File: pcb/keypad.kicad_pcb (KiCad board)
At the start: 2 copper layers, 148 x 103 mm, 54 parts, among them J1 Conn_02x06_Odd_Even, SW1 SW_Push, SW10 SW_Push, SW11 SW_Push, SW12 SW_Push, SW13 SW_Push, SW14 SW_Push, SW15 SW_Push, SW16 SW_Push, SW17 SW_Push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

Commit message: - Added a reset button for the controller  - Moved the through-hole diodes to not interfere with the switches
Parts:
- added SW_RST1: SW_Push, Button_Switch_THT:SW_PUSH_6mm_H7.3mm, F.Cu at (74.8, 18.0)
- moved D15 14.6 mm to (59.0, 93.8), turned to 90 degrees
- moved D19 14.3 mm to (140.0, 93.8), turned to 90 degrees
- moved D16 13.0 mm to (79.0, 93.8), turned to 90 degrees
- moved D17 12.9 mm to (98.0, 93.8), turned to 90 degrees
- moved D18 12.9 mm to (117.0, 93.8), turned to 90 degrees
- moved D20 2.85 mm to (56.0, 114.0)
- moved D21 2.85 mm to (85.2, 114.0)
- moved D22 2.85 mm to (114.4, 114.0)
- moved D1 2.00 mm to (28.0, 56.0)
- moved D2 2.00 mm to (47.1, 56.0)
- moved D3 2.00 mm to (66.1, 56.0)
- moved D4 2.00 mm to (85.2, 56.0)
- moved D5 2.00 mm to (104.2, 56.0)
- moved D6 2.00 mm to (123.3, 56.0)
- moved D7 2.00 mm to (142.3, 56.0)
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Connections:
- net /3.3v renamed /5v
- U1 pad 22: unconnected-(U1-Pad22) -> Net-(U1-Pad22)
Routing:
- net Net-(U1-Pad22): track 0.00 -> 85.2 mm
- net /Col2: track 223.5 -> 211.7 mm
- net /Col3: track 214.9 -> 206.8 mm
- net /Col1: track 299.3 -> 305.4 mm
- net /Col0: track 239.4 -> 245.2 mm
- net Net-(D18-Pad2): track 12.3 -> 6.81 mm
- net Net-(D17-Pad2): track 12.3 -> 6.83 mm
- net Net-(D16-Pad2): track 12.3 -> 6.85 mm
- net Net-(D15-Pad2): track 12.4 -> 7.51 mm
- net Net-(D19-Pad2): track 12.3 -> 7.39 mm
- net Net-(D22-Pad2): track 12.3 -> 15.3 mm
- net Net-(D21-Pad2): track 12.3 -> 15.1 mm
- net Net-(D20-Pad2): track 12.3 -> 15.1 mm
- net /Col5: track 156.7 -> 154.7 mm
- net Net-(D7-Pad2): track 12.3 -> 14.3 mm
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
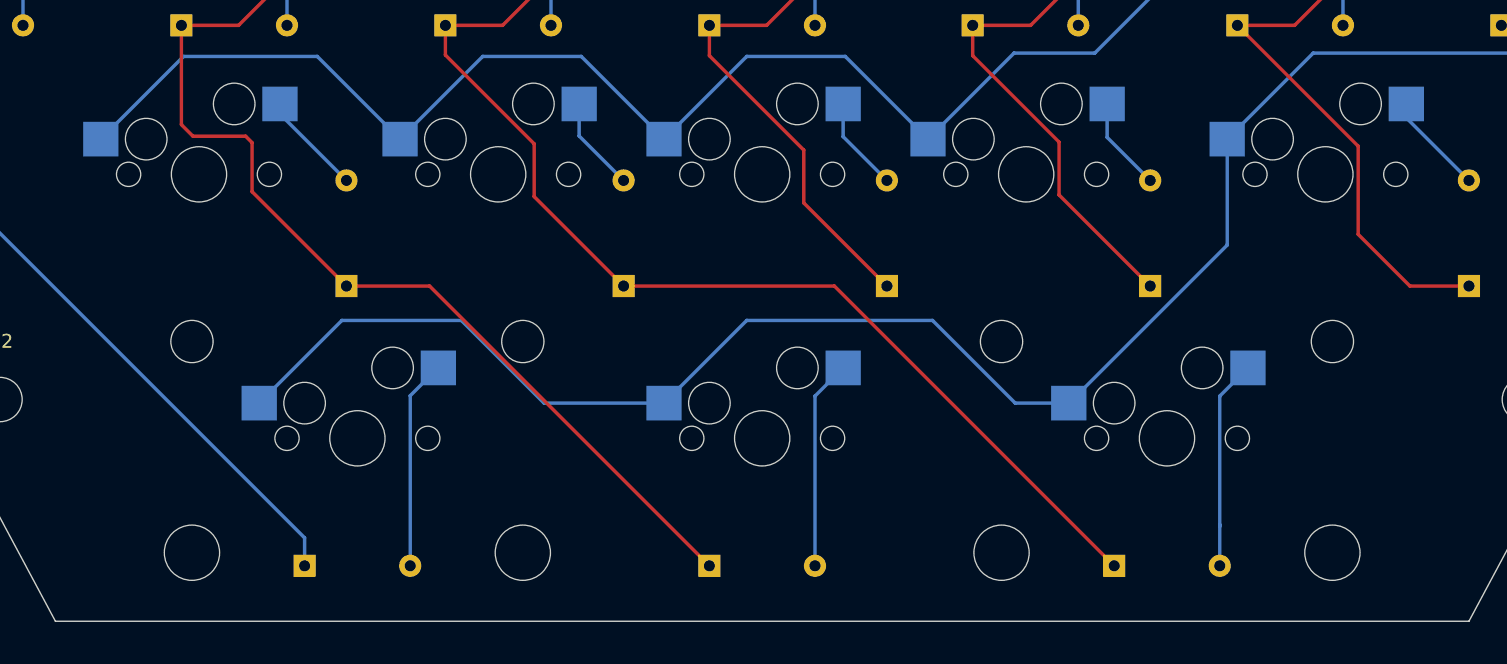
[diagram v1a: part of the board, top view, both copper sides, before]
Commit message: - Added plate details  - Fixed the spacing of non-1U keys on the PCB layout
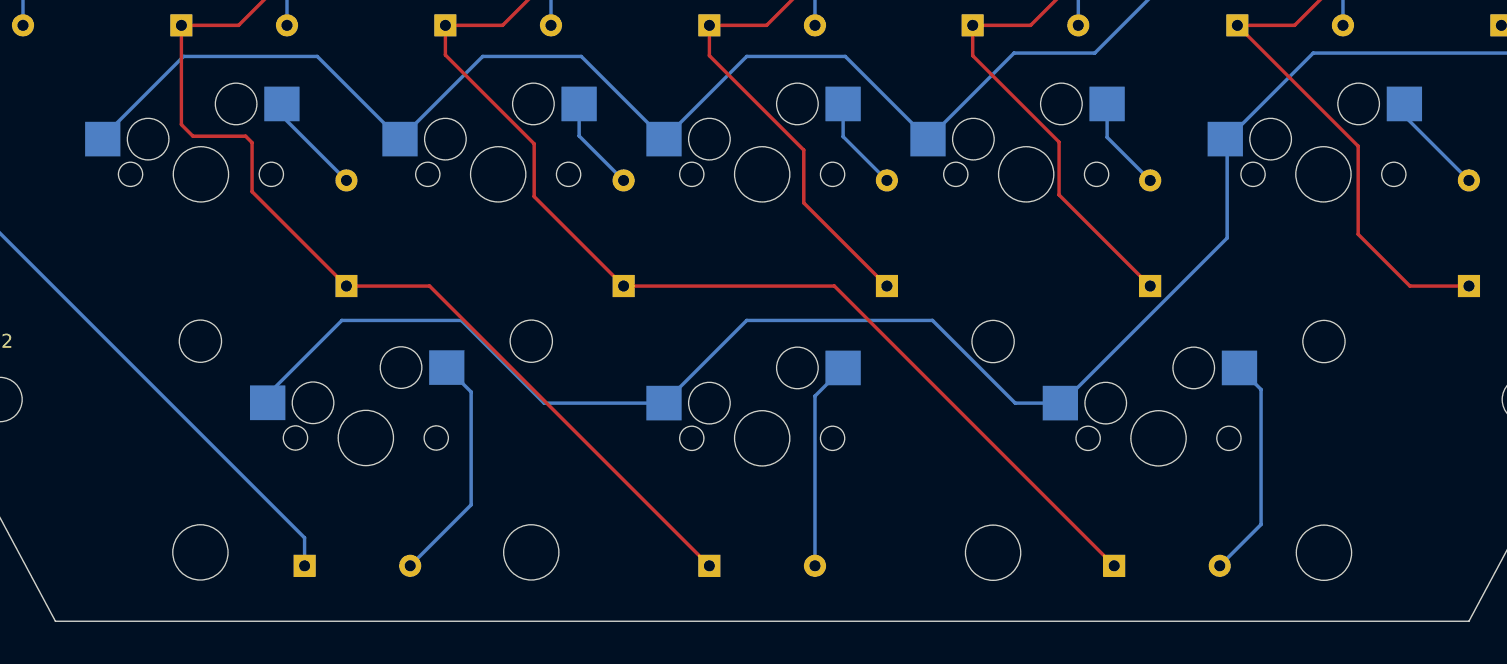
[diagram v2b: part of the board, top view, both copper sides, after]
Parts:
- moved SW20 0.61 mm to (60.4, 104.8)
- moved SW22 0.61 mm to (117.6, 104.8)
- moved SW15 0.14 mm to (48.5, 85.8)
- moved SW19 0.14 mm to (129.5, 85.8)
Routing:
- net Net-(D20-Pad2): track 15.1 -> 16.9 mm
- net Net-(D22-Pad2): track 15.3 -> 16.2 mm
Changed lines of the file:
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@@
   (net 22 "unconnected-(U1-Pad24)")
   (net 23 "/GND")
-  (net 24 "Net-(U1-Pad22)")
+  (net 24 "Net-(SW_RST1-Pad1)")
   (net 25 "unconnected-(U1-Pad1)")
   (net 26 "Net-(D10-Pad2)")
@@
   (net 48 "unconnected-(U1-Pad20)")
   (footprint "MX_Only:MXOnly-2U-Hotswap" (layer "F.Cu")
-    (at 59.79 104.8)
+    (at 60.4 104.77555)
     (property "Sheetfile" "keypad.kicad_sch")
     (property "Sheetname" "")
@@
   )
   (footprint "MX_Only:MXOnly-1.25U-Hotswap" (layer "F.Cu")
-    (at 48.36 85.75)
+    (at 48.5 85.75)
     (property "Sheetfile" "keypad.kicad_sch")
     (property "Sheetname" "")
@@
     (fp_circle (center 3.25 2.25) (end 1.25 2.5) (layer "F.Fab") (width 0.1) (fill none))
     (pad "1" thru_hole circle (at 6.5 0 90) (size 2 2) (drill 1.1) (layers *.Cu *.Mask)
-      (net 24 "Net-(U1-Pad22)") (pinfunction "1") (pintype "passive"))
+      (net 24 "Net-(SW_RST1-Pad1)") (pinfunction "1") (pintype "passive"))
     (pad "1" thru_hole circle (at 0 0 90) (size 2 2) (drill 1.1) (layers *.Cu *.Mask)
-      (net 24 "Net-(U1-Pad22)") (pinfunction "1") (pintype "passive"))
+      (net 24 "Net-(SW_RST1-Pad1)") (pinfunction "1") (pintype "passive"))
     (pad "2" thru_hole circle (at 0 4.5 90) (size 2 2) (drill 1.1) (layers *.Cu *.Mask)
       (net 23 "/GND") (pinfunction "2") (pintype "passive"))
@@
   )
   (footprint "MX_Only:MXOnly-2U-Hotswap" (layer "F.Cu")
-    (at 118.21 104.8)
+    (at 117.6 104.8)
     (property "Sheetfile" "keypad.kicad_sch")
     (property "Sheetname" "")
@@
   )
   (footprint "MX_Only:MXOnly-1.25U-Hotswap" (layer "F.Cu")
-    (at 129.64 85.75)
+    (at 129.5 85.75)
     (property "Sheetfile" "keypad.kicad_sch")
     (property "Sheetname" "")
@@
       (net 21 "/5v") (pinfunction "VCC") (pintype "power_in"))
     (pad "22" thru_hole oval locked (at 0 22.86 90) (size 1.6 1.6) (drill 0.8) (layers *.Cu *.Mask)
-      (net 24 "Net-(U1-Pad22)") (pinfunction "RST") (pintype "input"))
+      (net 24 "Net-(SW_RST1-Pad1)") (pinfunction "RST") (pintype "input"))
     (pad "23" thru_hole oval locked (at 0 25.4 90) (size 1.6 1.6) (drill 0.8) (layers *.Cu *.Mask)
       (net 23 "/GND") (pinfunction "GND") (pintype "power_in"))
@@
   (segment (start 90.5 18) (end 97 18) (width 0.25) (layer "B.Cu") (net 18))
   (segment (start 128.765 77) (end 122.555 83.21) (width 0.25) (layer "B.Cu") (net 18))
+  (segment (start 122.555 90.345) (end 122.555 83.21) (width 0.25) (layer "B.Cu") (net 18))
+  (segment (start 122.555 90.345) (end 110.64 102.26) (width 0.25) (layer "B.Cu") (net 18))
   (segment (start 135.45 20.45) (end 135.55 20.45) (width 0.25) (layer "B.Cu") (net 18))
   (segment (start 121.365 29) (end 121.365 37.728604) (width 0.25) (layer "B.Cu") (net 18))
@@
   (segment (start 135.45 20.45) (end 129.915 20.45) (width 0.25) (layer "B.Cu") (net 18))
   (segment (start 128 24) (end 131.55 20.45) (width 0.25) (layer "B.Cu") (net 18))
-  (segment (start 122.555 90.855) (end 122.555 83.21) (width 0.25) (layer "B.Cu") (net 18))
   (segment (start 152.109188 38.1) (end 154.042 40.032812) (width 0.25) (layer "B.Cu") (net 18))
-  (segment (start 111.15 102.26) (end 122.555 90.855) (width 0.25) (layer "B.Cu") (net 18))
   (segment (start 121.736396 38.1) (end 152.109188 38.1) (width 0.25) (layer "B.Cu") (net 18))
   (segment (start 58.673302 96.291698) (end 67.291698 96.291698) (width 0.25) (layer "B.Cu") (net 18))
@@
   (segment (start 67.291698 96.291698) (end 73.26 102.26) (width 0.25) (layer "B.Cu") (net 18))
   (segment (start 131.55 20.45) (end 135.45 20.45) (width 0.25) (layer "B.Cu") (net 18))
-  (segment (start 111.125 102.26) (end 111.15 102.26) (width 0.25) (layer "B.Cu") (net 18))
   (segment (start 101.291698 96.291698) (end 107.26 102.26) (width 0.25) (layer "B.Cu") (net 18))
   (segment (start 107.26 102.26) (end 111.125 102.26) (width 0.25) (layer "B.Cu") (net 18))
   (segment (start 87.883302 96.291698) (end 101.291698 96.291698) (width 0.25) (layer "B.Cu") (net 18))
+  (segment (start 110.64 102.26) (end 110.515 102.26) (width 0.25) (layer "B.Cu") (net 18))
   (segment (start 97 18) (end 101.5 18) (width 0.25) (layer "B.Cu") (net 18))
   (segment (start 149.550991 77) (end 128.765 77) (width 0.25) (layer "B.Cu") (net 18))
@@
   (segment (start 135.482 81.672) (end 135.482 80.67) (width 0.25) (layer "B.Cu") (net 35))
   (segment (start 140 86.19) (end 135.482 81.672) (width 0.25) (layer "B.Cu") (net 35))
-  (segment (start 65.632 99.72) (end 65.607 99.72) (width 0.25) (layer "B.Cu") (net 36))
-  (segment (start 65.607 99.72) (end 63.6 101.727) (width 0.25) (layer "B.Cu") (net 36))
-  (segment (start 63.6 101.727) (end 63.6 114) (width 0.25) (layer "B.Cu") (net 36))
+  (segment (start 68 101.45355) (end 68 109.6) (width 0.25) (layer "B.Cu") (net 36))
+  (segment (start 68 109.6) (end 63.6 114) (width 0.25) (layer "B.Cu") (net 36))
+  (segment (start 66.242 99.69555) (end 68 101.45355) (width 0.25) (layer "B.Cu") (net 36))
   (segment (start 108 25.69) (end 108.56 26.25) (width 0.25) (layer "B.Cu") (net 37))
   (segment (start 108 22.5) (end 108 25.69) (width 0.25) (layer "B.Cu") (net 37))
@@
   (segment (start 56.742 61.62) (end 54.71 63.652) (width 0.25) (layer "B.Cu") (net 39))
   (segment (start 54.71 63.652) (end 54.71 75) (width 0.25) (layer "B.Cu") (net 39))
-  (segment (start 122.02 101.752) (end 122.02 111.15) (width 0.25) (layer "B.Cu") (net 40))
-  (segment (start 122.02 114) (end 122.02 111.02) (width 0.25) (layer "B.Cu") (net 40))
-  (segment (start 124.052 99.72) (end 122.02 101.752) (width 0.25) (layer "B.Cu") (net 40))
+  (segment (start 125 111.02) (end 122.02 114) (width 0.25) (layer "B.Cu") (net 40))
+  (segment (start 123.442 99.72) (end 125 101.278) (width 0.25) (layer "B.Cu") (net 40))
+  (segment (start 125 101.278) (end 125 111.02) (width 0.25) (layer "B.Cu") (net 40))
   (segment (start 97 22.5) (end 97 25.69) (width 0.25) (layer "B.Cu") (net 43))
   (segment (start 97 25.69) (end 97.56 26.25) (width 0.25) (layer "B.Cu") (net 43))

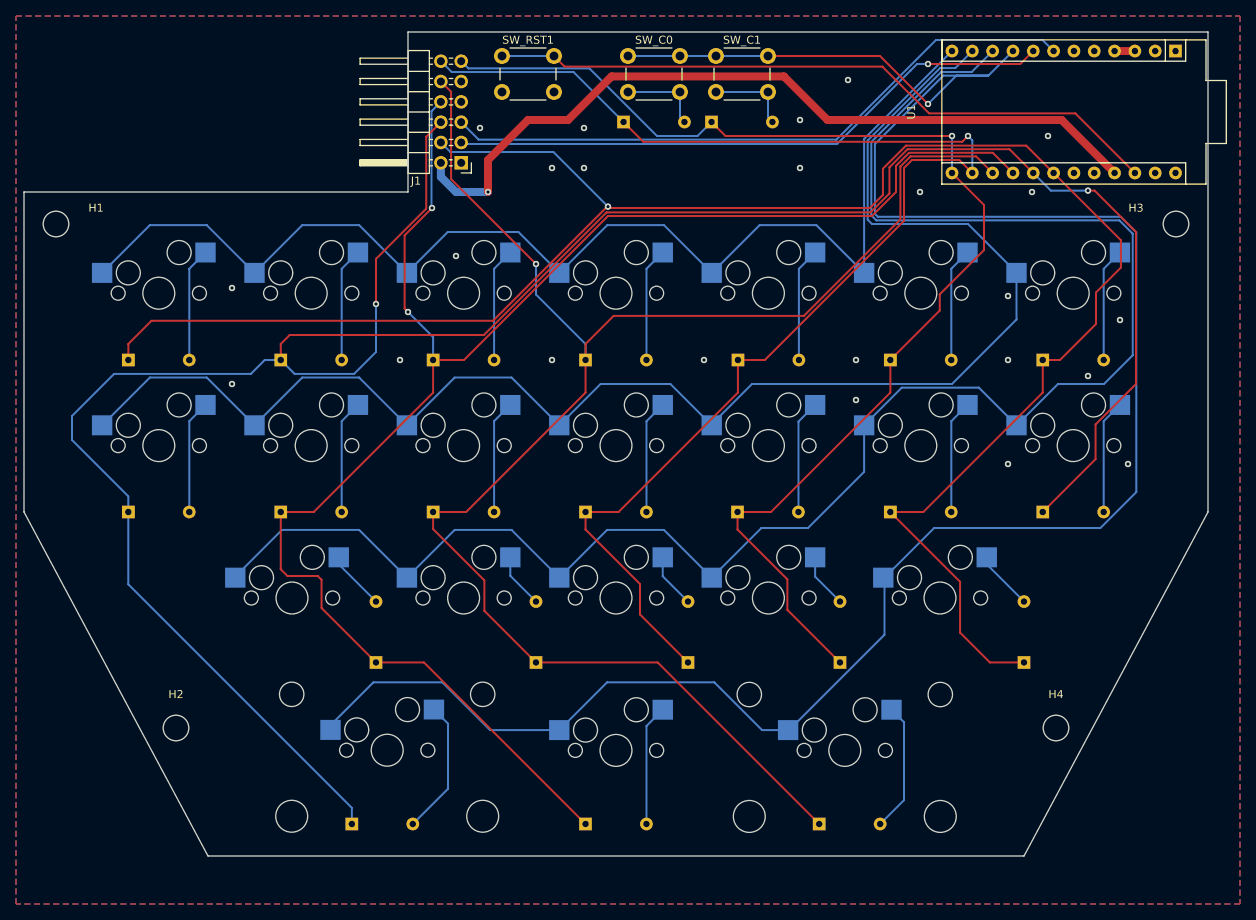
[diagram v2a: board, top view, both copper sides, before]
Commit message: - Switched to the KB2040  - Modified the pin header to remove some silk screen sections
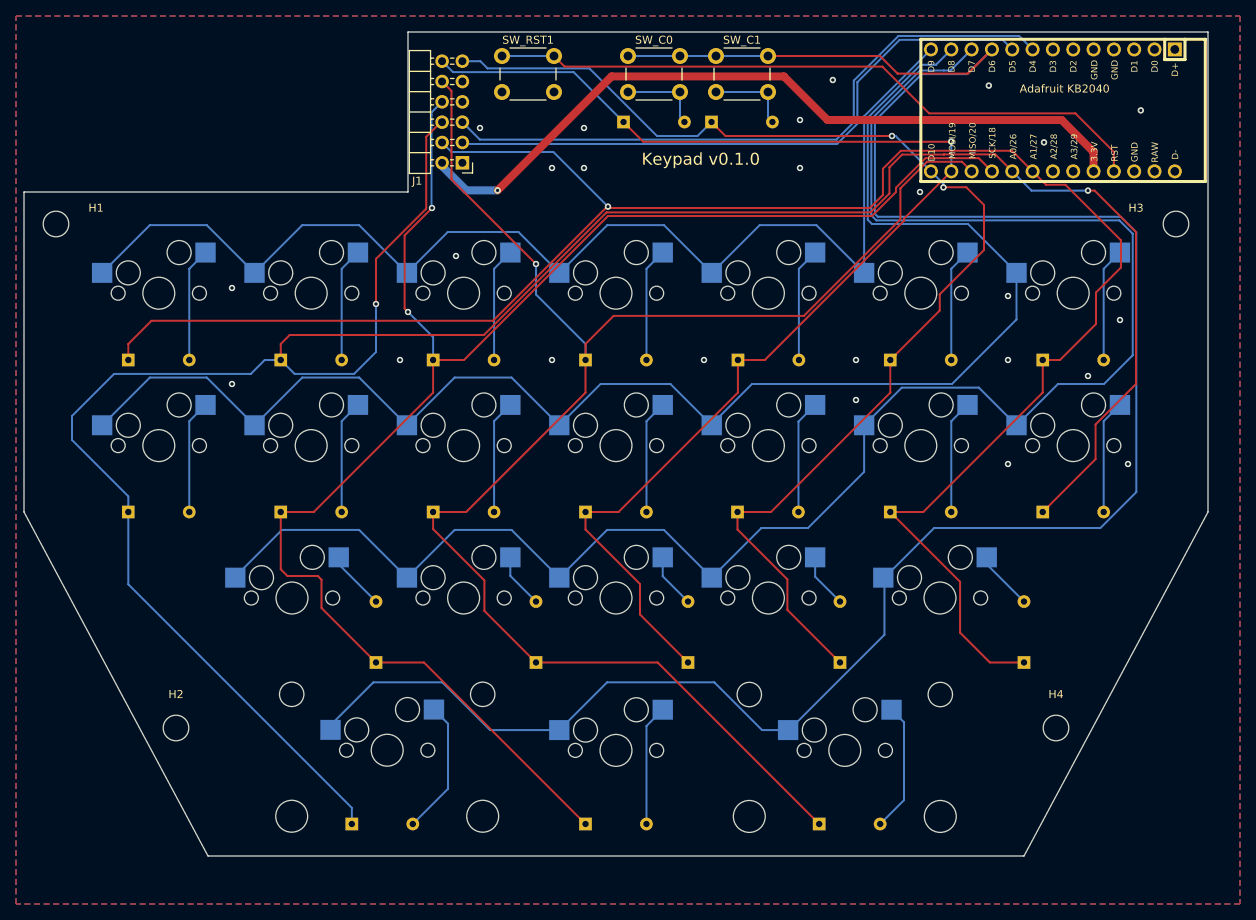
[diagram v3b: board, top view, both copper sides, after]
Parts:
- J1: footprint Connector_PinHeader_2.54mm:PinHeader_2x06_P2.54mm_Horizontal -> keypad:PinHeader_2x06_P2.54mm_Horizontal
- U1: value Sparkfun_Pro_Micro -> kb2040; footprint Arduino:Sparkfun_Pro_Micro -> kb2040:kb2040
- moved U1 15.9 mm to (144.9, 24.8), turned to -90 degrees
- moved J1 0.15 mm to (69.8, 31.4)
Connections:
- J1 pad 2: /5v -> /3.3v
- U1 pad 10: /Row2 -> /Row3
- U1 pad 11: /Row1 -> /Row2
- U1 pad 12: /Row0 -> /Row1
- U1 pad 13: /Col5 -> /Row0
- U1 pad 14: /Col4 -> unconnected-(U1-Pad14)
- U1 pad 15: /Col3 -> unconnected-(U1-Pad15)
- U1 pad 16: /Col2 -> /GND
- U1 pad 17: /Col1 -> Net-(SW_RST1-Pad1)
- U1 pad 18: /Col0 -> /3.3v
- U1 pad 21: /5v -> /Col0
- U1 pad 22: Net-(SW_RST1-Pad1) -> /Col1
- U1 pad 23: /GND -> /Col2
- U1 pad 24: unconnected-(U1-Pad24) -> /Col3
- U1 pad 3: /GND -> unconnected-(U1-Pad3)
- U1 pad 5: unconnected-(U1-Pad5) -> /GND
- U1 pad 7: /Row5 -> unconnected-(U1-Pad7)
- U1 pad 8: /Row4 -> /Row5
- U1 pad 9: /Row3 -> /Row4
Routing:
- net /5v: track 100.1 -> 0.00 mm, vias 1 -> 0
- net /3.3v: track 0.00 -> 95.3 mm, vias 0 -> 1
- net /Col4: track 172.8 -> 161.6 mm
- net /Col3: track 206.8 -> 202.0 mm
- net /Col2: track 211.7 -> 206.9 mm
- net /GND: track 2.54 -> 0.00 mm, vias 24 -> 25
- net /Col5: track 154.7 -> 152.1 mm, vias 1 -> 2
- net /Row3: track 274.1 -> 272.1 mm, vias 1 -> 0
- net /Row4: track 76.4 -> 78.0 mm, vias 1 -> 0
- net Net-(SW_RST1-Pad1): track 85.2 -> 83.9 mm
- net /Row2: track 223.8 -> 223.0 mm
- net /Row1: track 193.8 -> 192.9 mm
- net /Row0: track 151.5 -> 150.7 mm
- net /Col0: track 245.2 -> 244.5 mm
- net /Row5: track 80.7 -> 81.3 mm
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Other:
- board text added: "Keypad v0.1.0"

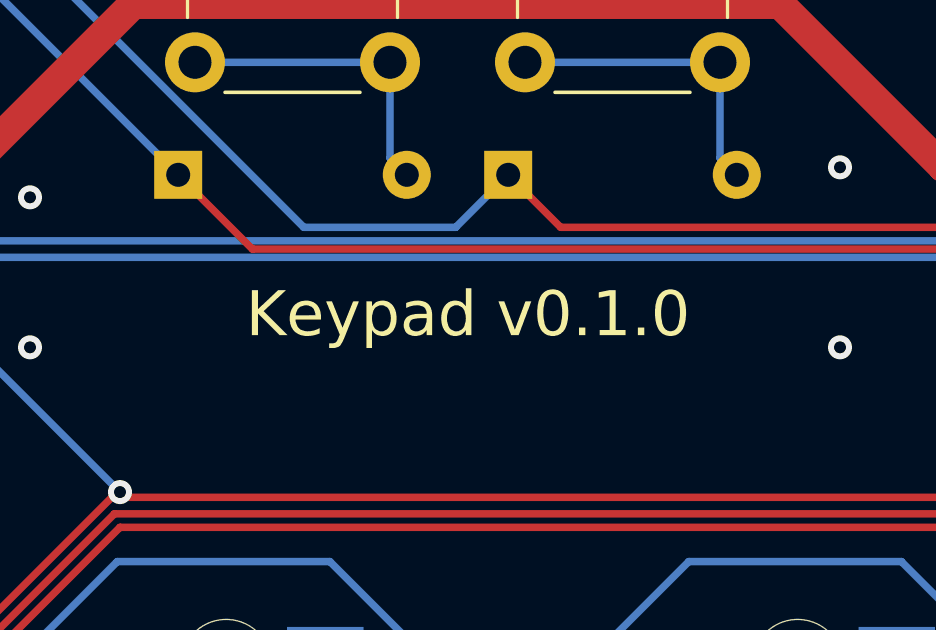
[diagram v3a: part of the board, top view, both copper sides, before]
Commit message: Moved necessary symbols into the project library  - (I don't know if this comes with license issues; if there's a problem let me know and I can remove the symbols)
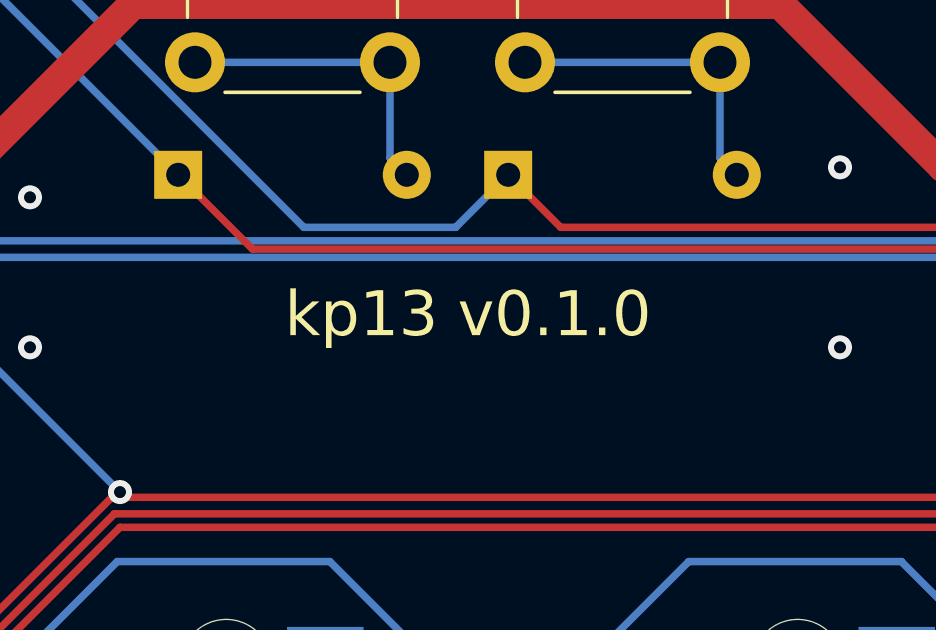
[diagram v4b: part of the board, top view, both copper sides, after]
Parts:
- SW1, SW10, SW11, SW12, SW13, SW14, SW16, SW17, SW18, SW2, SW21, SW3, SW4, SW5, SW6, SW7, SW8, SW9: footprint MX_Only:MXOnly-1U-Hotswap -> keypad:MXOnly-1U-Hotswap
- SW15, SW19: footprint MX_Only:MXOnly-1.25U-Hotswap -> keypad:MXOnly-1.25U-Hotswap
- SW20, SW22: footprint MX_Only:MXOnly-2U-Hotswap -> keypad:MXOnly-2U-Hotswap
- U1: value kb2040 -> ProMicro; footprint kb2040:kb2040 -> keypad:kb2040
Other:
- board text added: "kp13 v0.1.0"
- board text removed: "Keypad v0.1.0"
